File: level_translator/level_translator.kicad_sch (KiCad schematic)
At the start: 5 parts, among them J1 Conn_01x05_Male, J2 Conn_01x05_Female, U1 pi141x3x

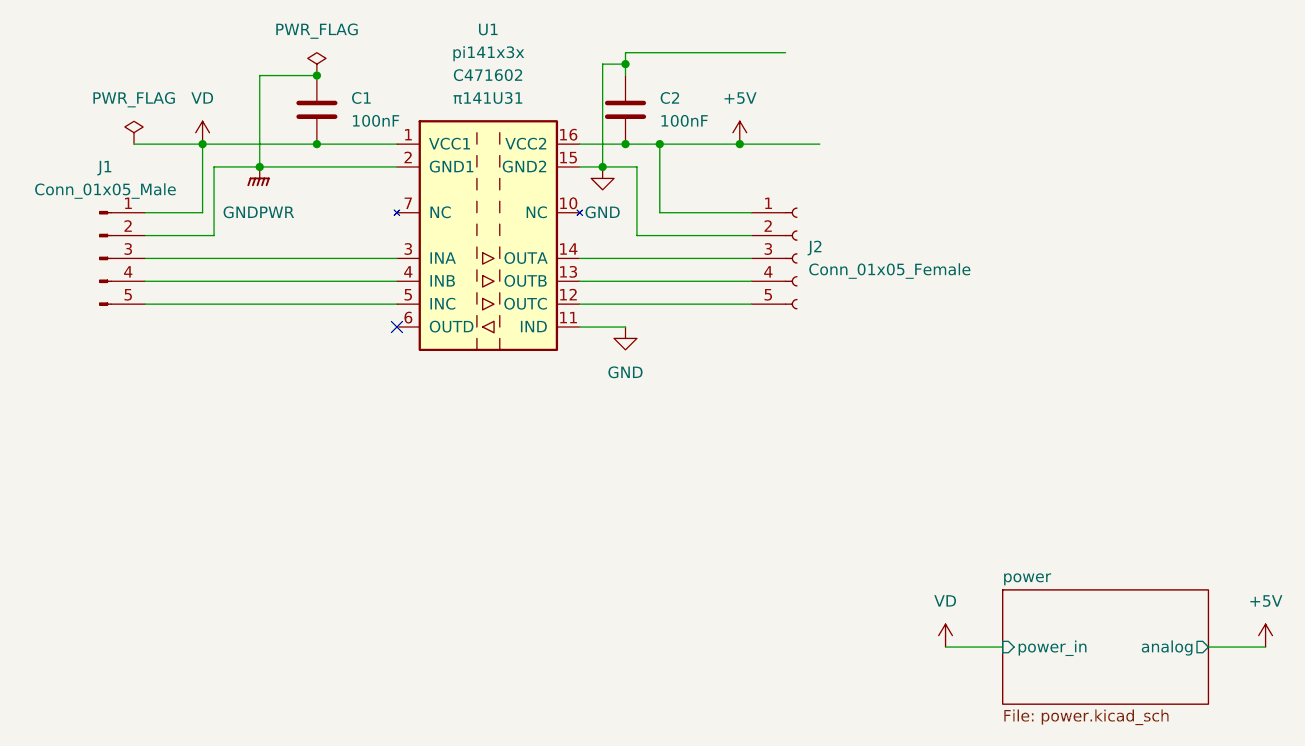
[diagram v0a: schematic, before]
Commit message: Add tweaks to diode readout
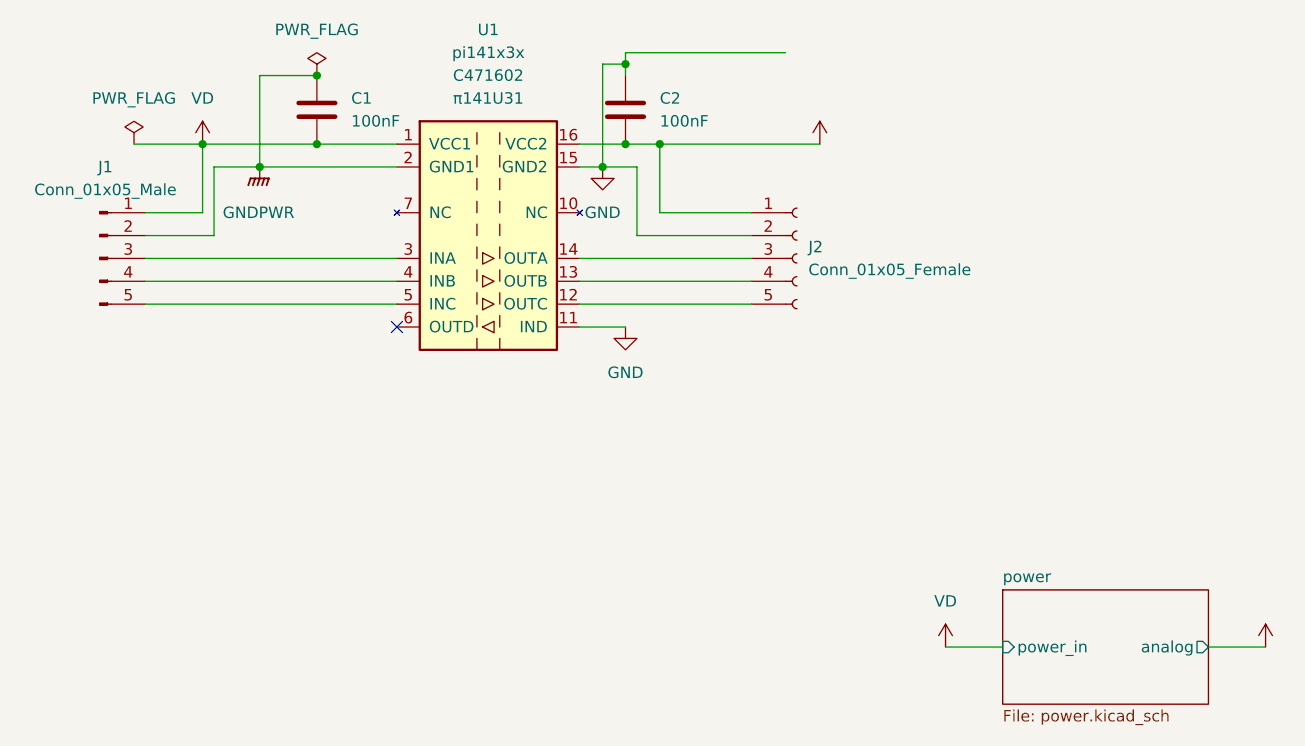
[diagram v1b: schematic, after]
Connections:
- net +5V renamed +4.5V
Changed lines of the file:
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@@
   (junction (at 138.43 31.75) (diameter 0) (color 0 0 0 0)
-  )
-  (junction (at 151.13 40.64) (diameter 0) (color 0 0 0 0)
   )
   (junction (at 91.44 40.64) (diameter 0) (color 0 0 0 0)
@@
     (stroke (width 0) (type default) (color 0 0 0 0))
   )
-  (wire (pts (xy 142.24 40.64) (xy 151.13 40.64))
-    (stroke (width 0) (type default) (color 0 0 0 0))
-  )
   (wire (pts (xy 138.43 31.75) (xy 135.89 31.75))
     (stroke (width 0) (type default) (color 0 0 0 0))
@@
     (stroke (width 0) (type default) (color 0 0 0 0))
   )
-  (wire (pts (xy 160.02 40.64) (xy 151.13 40.64))
+  (wire (pts (xy 142.24 40.64) (xy 160.02 40.64))
     (stroke (width 0) (type default) (color 0 0 0 0))
   )
@@
     (stroke (width 0) (type default) (color 0 0 0 0))
   )
-  (symbol (lib_id "power:+5V") (at 151.13 40.64 0) (unit 1)
-    (in_bom yes) (on_board yes) (fields_autoplaced)
-    (property "Reference" "#PWR04" (id 0) (at 151.13 44.45 0)
-      (effects (font (size 1.27 1.27)) hide)
-    )
-    (property "Value" "+5V" (id 1) (at 151.13 35.56 0))
-    (property "Footprint" "" (id 2) (at 151.13 40.64 0)
-      (effects (font (size 1.27 1.27)) hide)
-    )
-    (property "Datasheet" "" (id 3) (at 151.13 40.64 0)
+  (symbol (lib_id "power:+4.5V") (at 209.55 96.52 0) (unit 1)
+    (in_bom yes) (on_board yes) (fields_autoplaced)
+    (property "Reference" "#PWR?" (id 0) (at 209.55 100.33 0)
+      (effects (font (size 1.27 1.27)) hide)
+    )
+    (property "Value" "" (id 1) (at 209.55 91.44 0))
+    (property "Footprint" "" (id 2) (at 209.55 96.52 0)
+      (effects (font (size 1.27 1.27)) hide)
+    )
+    (property "Datasheet" "" (id 3) (at 209.55 96.52 0)
       (effects (font (size 1.27 1.27)) hide)
     )
@@
     )
     (property "Datasheet" "~" (id 3) (at 104.14 33.02 0)
+      (effects (font (size 1.27 1.27)) hide)
+    )
+    (pin "1")
+  )
+  (symbol (lib_id "power:+4.5V") (at 160.02 40.64 0) (unit 1)
+    (in_bom yes) (on_board yes) (fields_autoplaced)
+    (property "Reference" "#PWR?" (id 0) (at 160.02 44.45 0)
+      (effects (font (size 1.27 1.27)) hide)
+    )
+    (property "Value" "" (id 1) (at 160.02 35.56 0))
+    (property "Footprint" "" (id 2) (at 160.02 40.64 0)
+      (effects (font (size 1.27 1.27)) hide)
+    )
+    (property "Datasheet" "" (id 3) (at 160.02 40.64 0)
       (effects (font (size 1.27 1.27)) hide)
     )
@@
     )
     (property "Datasheet" "" (id 3) (at 91.44 40.64 0)
-      (effects (font (size 1.27 1.27)) hide)
-    )
-    (pin "1")
-  )
-  (symbol (lib_id "power:+5V") (at 209.55 96.52 0) (unit 1)
-    (in_bom yes) (on_board yes) (fields_autoplaced)
-    (property "Reference" "#PWR06" (id 0) (at 209.55 100.33 0)
-      (effects (font (size 1.27 1.27)) hide)
-    )
-    (property "Value" "+5V" (id 1) (at 209.55 91.44 0))
-    (property "Footprint" "" (id 2) (at 209.55 96.52 0)
-      (effects (font (size 1.27 1.27)) hide)
-    )
-    (property "Datasheet" "" (id 3) (at 209.55 96.52 0)
       (effects (font (size 1.27 1.27)) hide)
     )
@@
       (reference "#PWR03") (unit 1) (value "GND") (footprint "")
     )
-    (path "/1b6cebf2-0b72-4812-88c6-f9254bcc593d"
-      (reference "#PWR04") (unit 1) (value "+5V") (footprint "")
-    )
     (path "/cf8afc3b-e83f-4eaa-be2d-c93c8056dbb7"
       (reference "#PWR05") (unit 1) (value "VD") (footprint "")
     )
-    (path "/be677d78-7229-4652-9bc9-3ba0893d9429"
-      (reference "#PWR06") (unit 1) (value "+5V") (footprint "")
-    )
     (path "/39954968-8f6d-4f30-a6bf-30427f2e3b5a/d82aff95-fb22-480d-86e7-a043b4d7eab7"
       (reference "#PWR07") (unit 1) (value "~") (footprint "")
@@
       (reference "#PWR0101") (unit 1) (value "GND") (footprint "")
     )
+    (path "/1c532554-e3f6-4e01-a2c0-98ff5e46b00d"
+      (reference "#PWR?") (unit 1) (value "+4.5V") (footprint "")
+    )
+    (path "/667e58fd-638b-48d8-8590-5f335cf78584"
+      (reference "#PWR?") (unit 1) (value "+4.5V") (footprint "")
+    )
     (path "/ed9c6735-a258-49b1-8520-ac27227c4247"
